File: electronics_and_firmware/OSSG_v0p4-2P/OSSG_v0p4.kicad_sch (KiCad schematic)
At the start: 35 parts, among them J1 Conn_01x05_Male, J2 Ext RGB, J4 Touch, Q1 2SC4617R BR, Q2 2SC4617R BR, SW1 SW_SPST, U1 MP23DB01HPTR, U2 ESP32-PICO-D4, U3 CH9102F

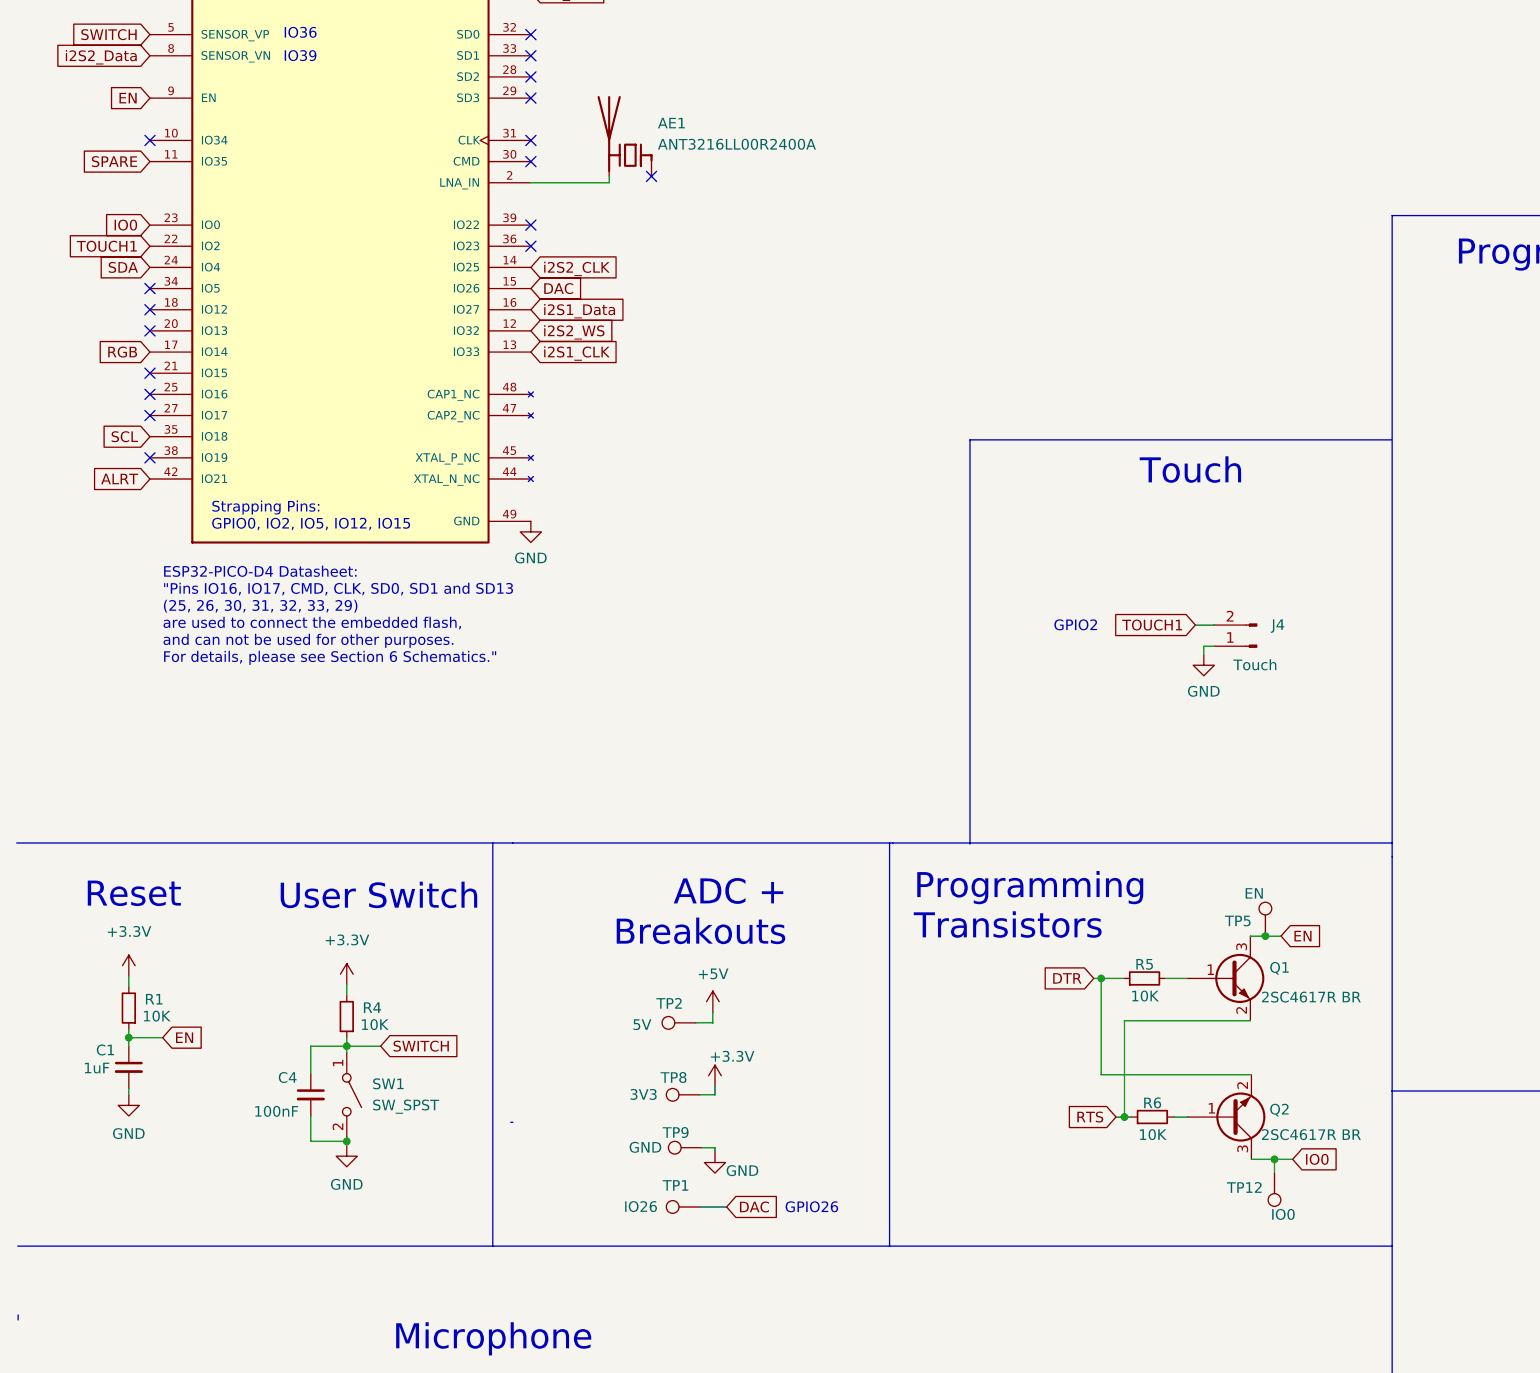
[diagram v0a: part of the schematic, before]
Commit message: ESP32 footprint edited, HUD connection, USB connector moved
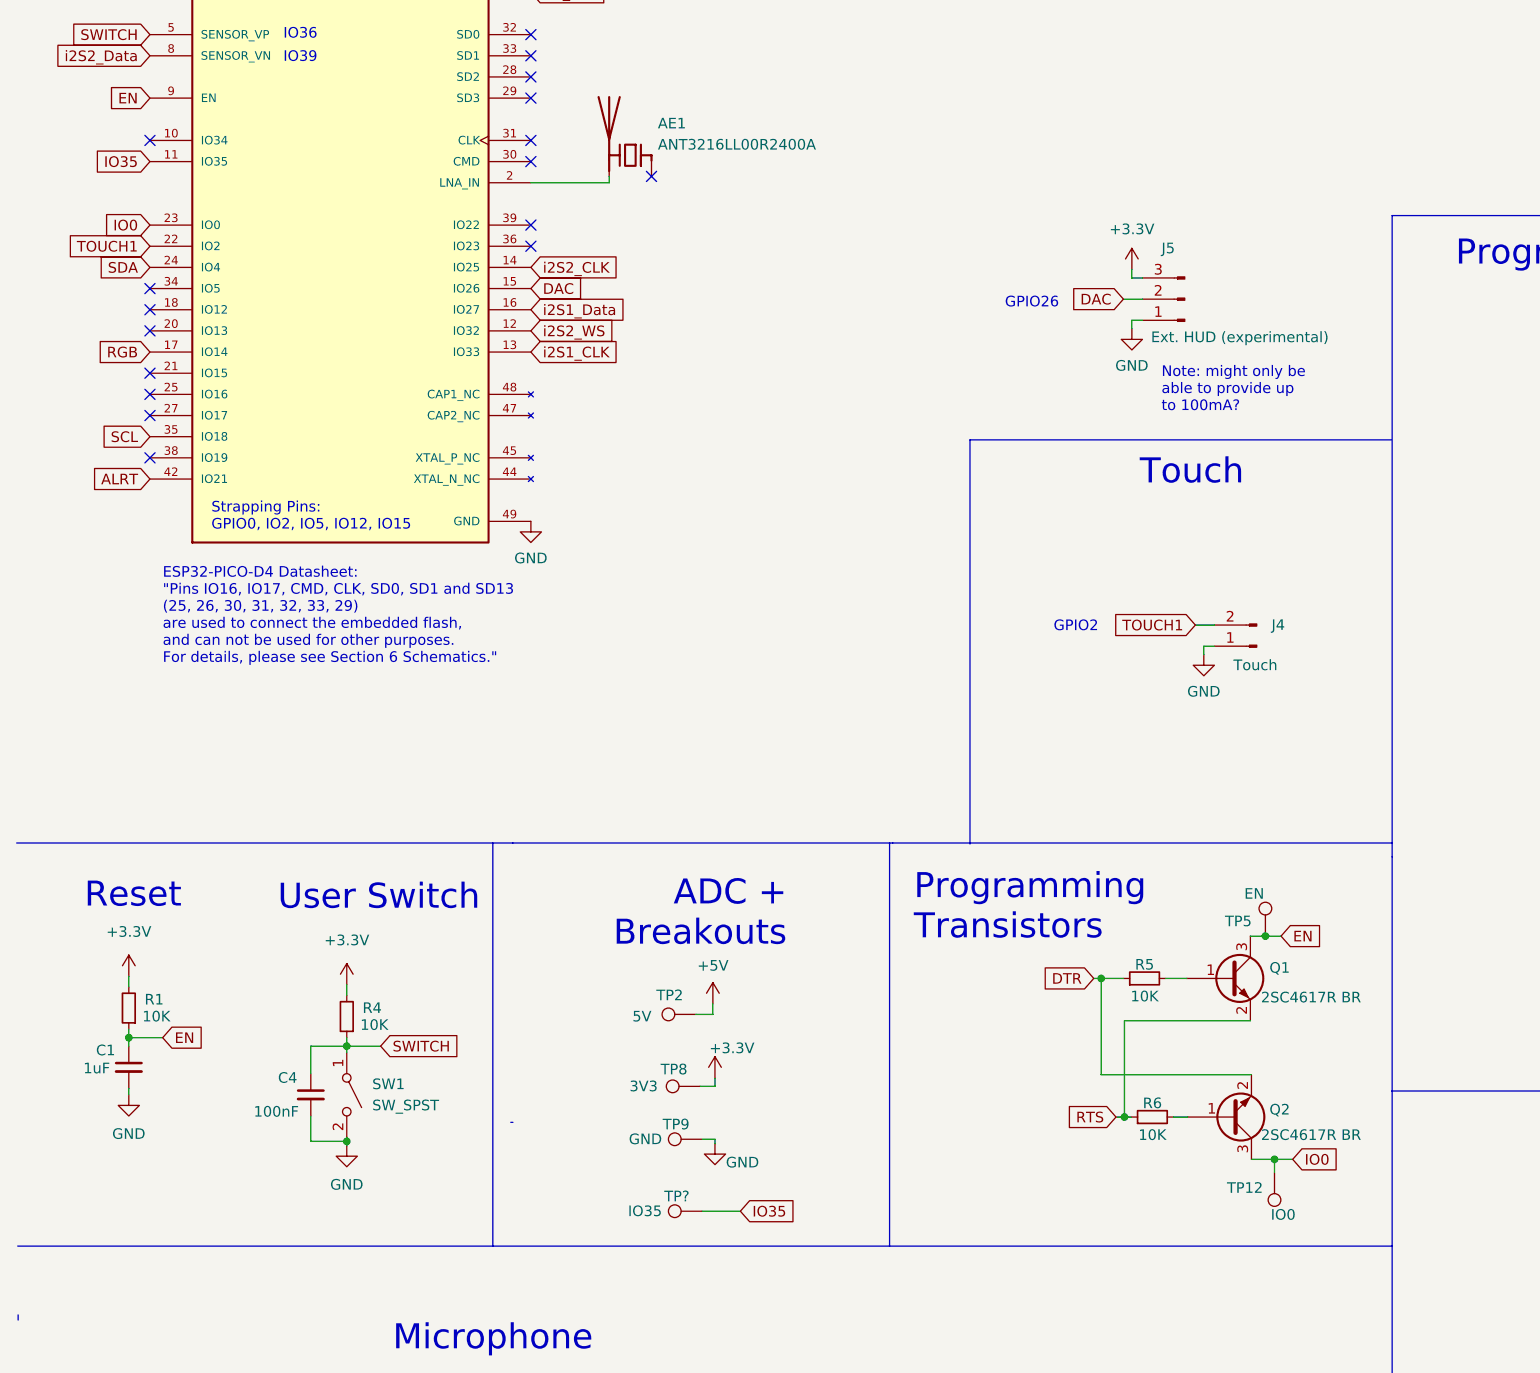
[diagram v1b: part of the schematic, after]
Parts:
- removed TP1: IO26, OSSG_footprints:Breakout_pads_very_small, symbol Connector:TestPoint
- added J5: Ext. HUD (experimental), OSSG_footprints:Solder-3P-Connector, symbol Connector:Conn_01x03_Male
- added TP?: IO35, OSSG_footprints:Breakout_pads_small, symbol Connector:TestPoint
- U2: footprint OSSG_footprints:ESP32_PICO_D4 -> OSSG_footprints:OSSG_ESP32-Pico_D4
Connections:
- net +3V3: now also J5.3 (Pin_3)
- net DAC: now also J5.2 (Pin_2)
- net GND: now also J5.1 (Pin_1)
- net SPARE renamed IO35
- net IO35: now also TP?.1
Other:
- note added: "Note: might only be able to provide up to 100mA?"
- moved on the sheet: TP2, TP8, TP9

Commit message: updating schematic and PCB with minor changes
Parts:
- gave numbers to parts that had none: 1
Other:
- note added: "Experimental"
- note added: "HUD"
- note added: "Left"
- note added: "Microphones"
- note added: "PDM (over i2S) Microphones"
- note added: "Right"
- note removed: "Microphone"
- moved on the sheet: J4, J5

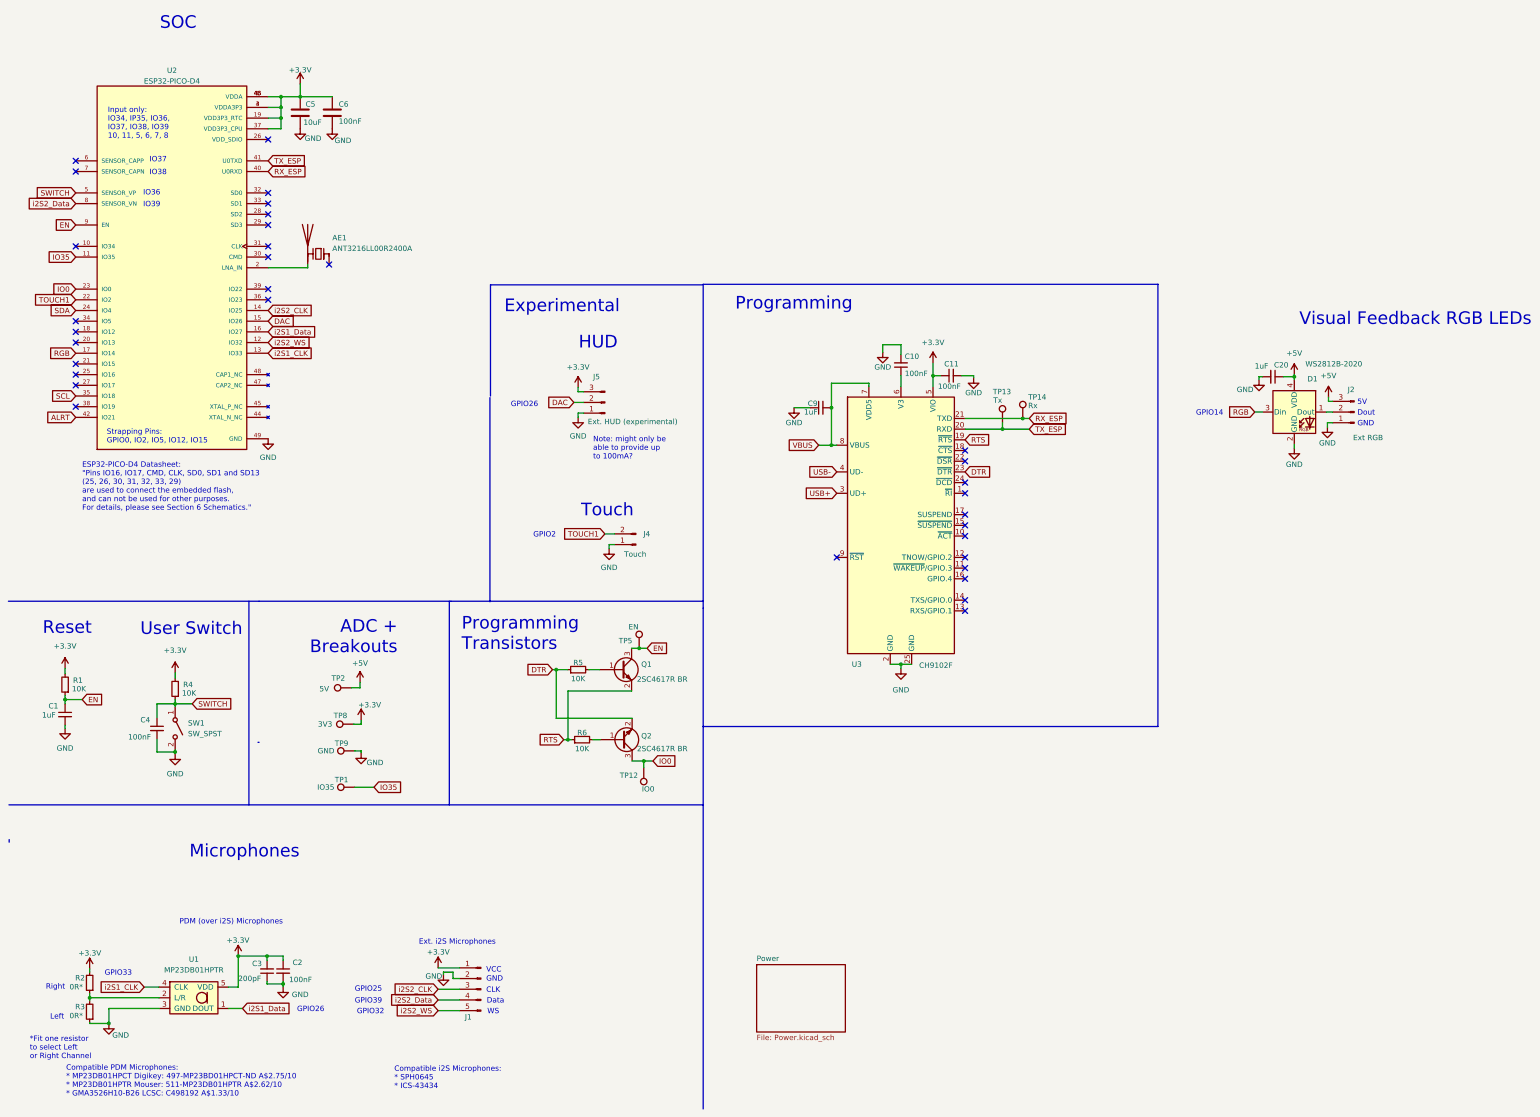
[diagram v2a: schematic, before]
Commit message: add PSRAM, move button to bottom (thumb press)
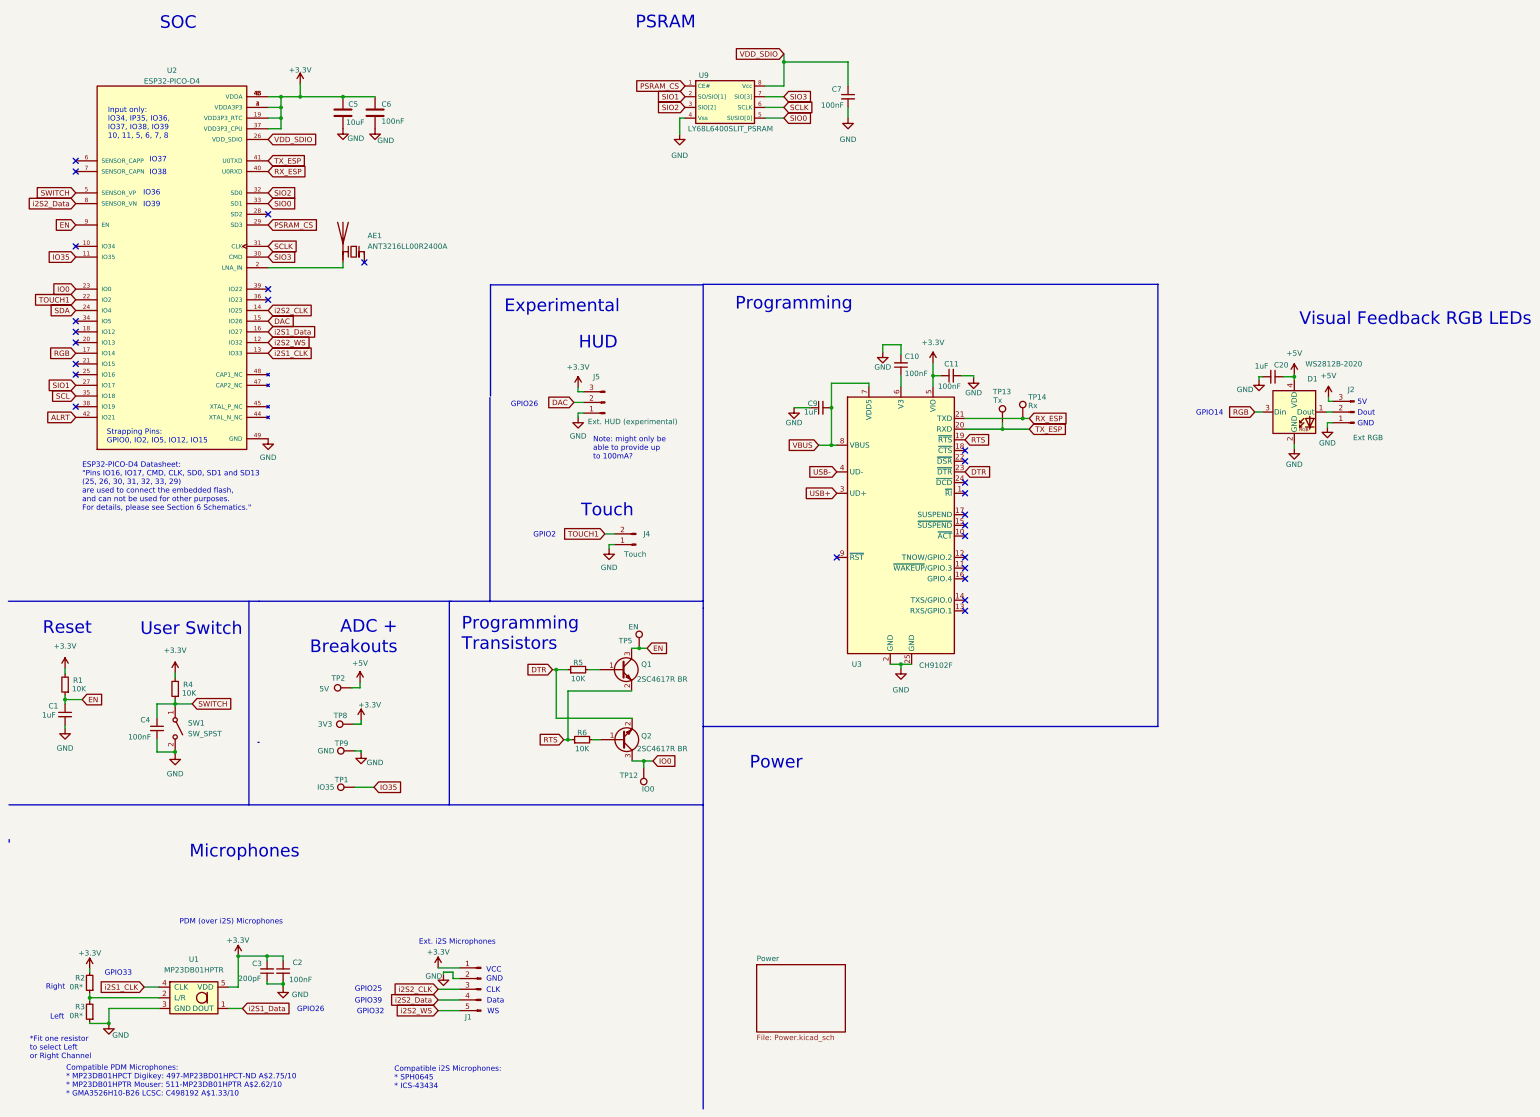
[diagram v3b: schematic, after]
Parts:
- added C7: 100nF, Capacitor_SMD:C_0402_1005Metric, symbol Device:C_Small
- added U9: LY68L6400SLIT_PSRAM, Package_SO:SOP-8_3.9x4.9mm_P1.27mm, symbol OSSG_components_lib:LY68L6400SLIT_PSRAM
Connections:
- net GND: now also C7.2, U9.4 (Vss)
- net VDD_SDIO: now reaches U2.26 (VDD_SDIO)
- net VDD_SDIO: now also C7.1, U9.8 (Vcc)
- net SIO1: now reaches U2.27 (IO17)
- net SIO1: now also U9.2 (SO/SIO[1])
- net PSRAM_CS: now reaches U2.29 (SD3)
- net PSRAM_CS: now also U9.1 (CE#)
- net SIO3: now reaches U2.30 (CMD)
- net SIO3: now also U9.7 (SIO[3])
- net SCLK: now reaches U2.31 (CLK)
- net SCLK: now also U9.6 (SCLK)
- net SIO2: now reaches U2.32 (SD0)
- net SIO2: now also U9.3 (SIO[2])
- net SIO0: now reaches U2.33 (SD1)
- net SIO0: now also U9.5 (SI/SIO[0])
- no-connect marks 33 -> 26
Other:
- note added: "PSRAM"
- note added: "Power"
- moved on the sheet: AE1, C5, C6
